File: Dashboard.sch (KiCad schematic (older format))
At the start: 24 parts, among them J24 ExtraGPIO_Conn, J25 UART_TP, J8 JTAG, SW10 RESET, U7 STM32F413RHTx, Y1 Crystal

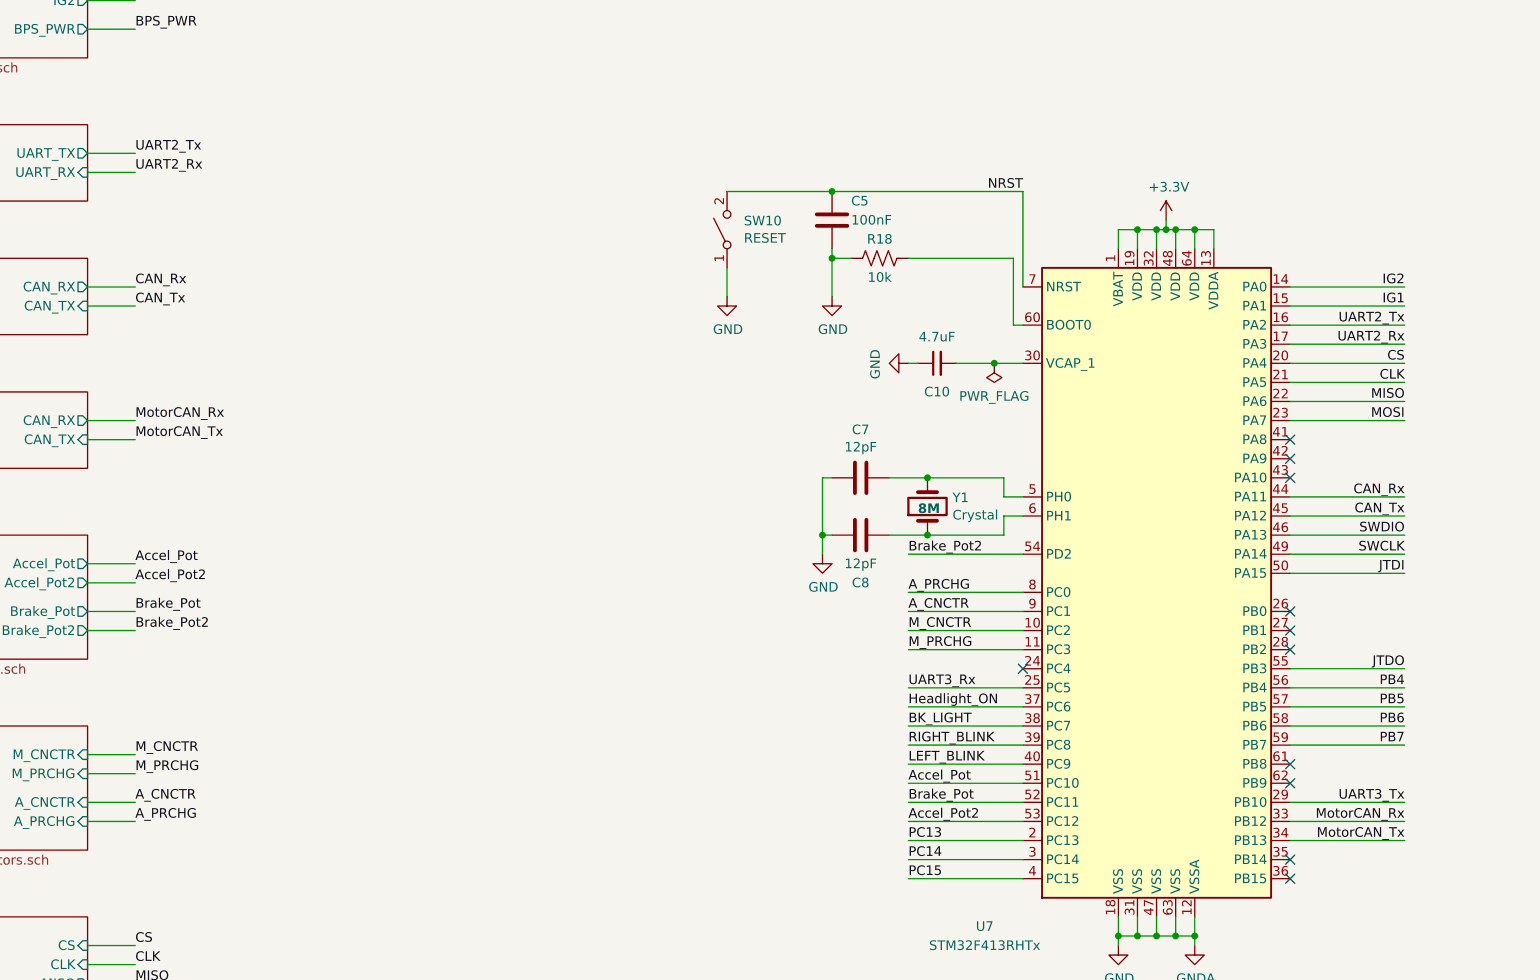
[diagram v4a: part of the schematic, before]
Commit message: USB Tx/Rx, Crystal Keepout, 12V Separation, Can2-Can3, Motor CAN bus labels, Power Input Protection Circuitry
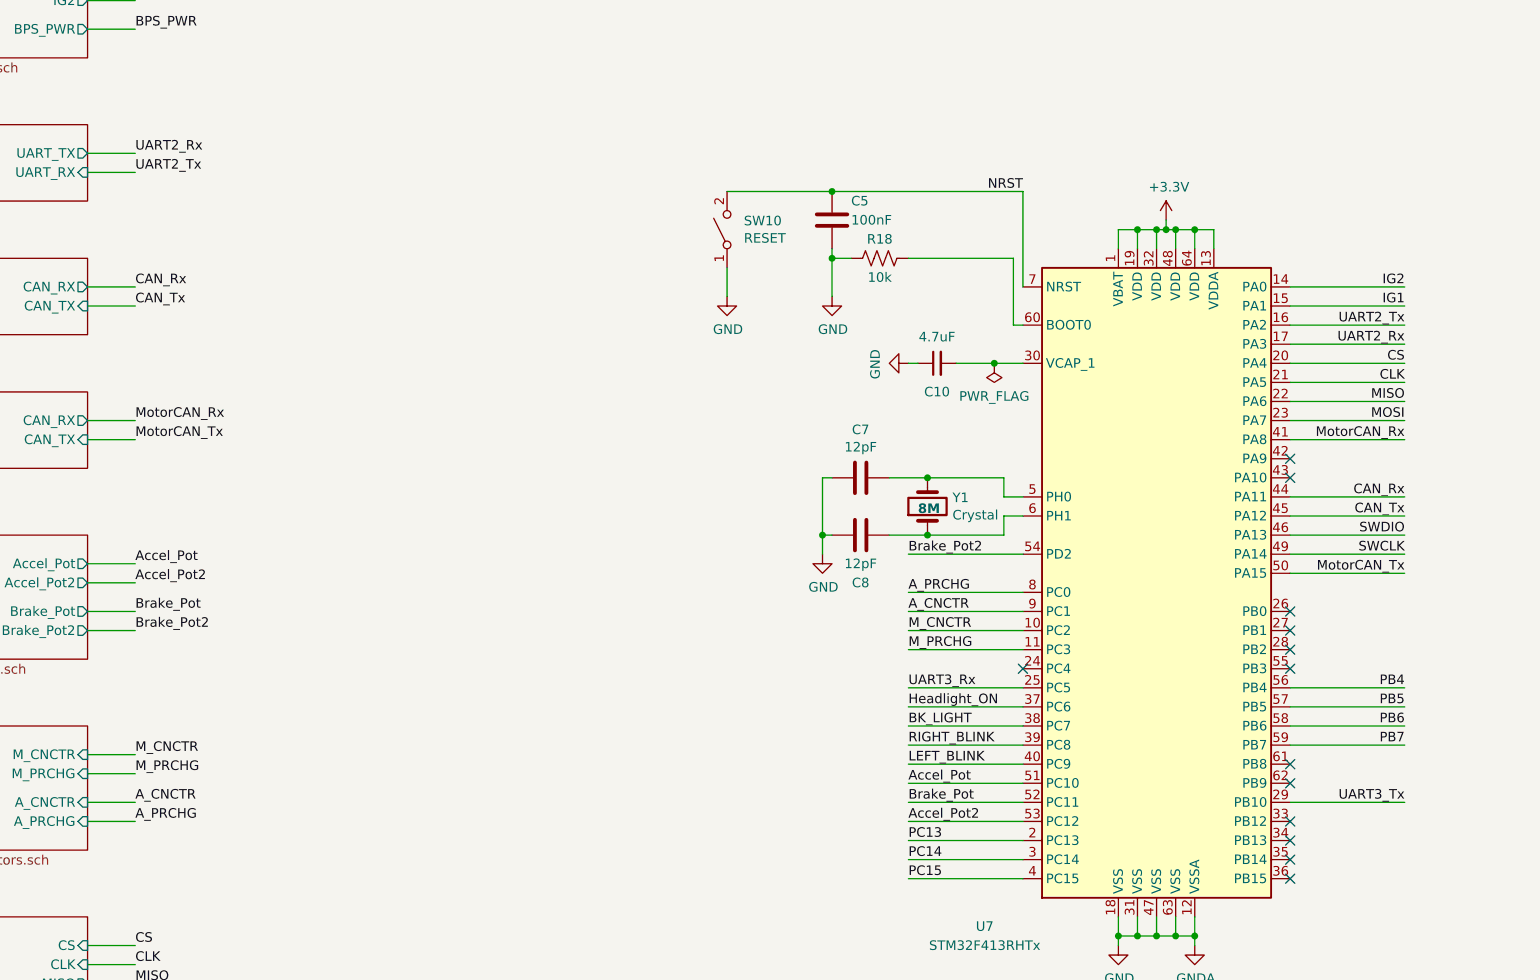
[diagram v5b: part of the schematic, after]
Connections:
- wire segments 169 -> 167
- no-connect marks 11 -> 13
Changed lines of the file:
@@
 Text Label 9600 6150 2    50   ~ 0
 SWCLK
-Text Label 9600 6250 2    50   ~ 0
-JTDI
-Text Label 9600 6750 2    50   ~ 0
-JTDO
 Wire Wire Line
 	9000 6150 9600 6150
@@
 	11900 4850 11900 5500
 Wire Wire Line
-	9000 6750 9600 6750
-Wire Wire Line
-	9000 6250 9600 6250
-Wire Wire Line
 	7000 6650 7600 6650
 Text Label 7000 6550 0    50   ~ 0
@@
 	8100 8150 8100 8200
 Connection ~ 8100 8150
-$Sheet
-S 1550 3900 1150 400
-U 5F7A9238
-F0 "USB" 50
-F1 "USB.sch" 50
-F2 "UART_RX" I R 2700 4150 50
-F3 "UART_TX" O R 2700 4050 50
-$EndSheet
 Wire Wire Line
 	7000 6850 7600 6850
-Text Label 2950 4050 0    50   ~ 0
+Text Label 2950 4150 0    50   ~ 0
 UART2_Tx
 Wire Wire Line
@@
 Wire Wire Line
 	2700 4150 2950 4150
-Text Label 2950 4150 0    50   ~ 0
+Text Label 2950 4050 0    50   ~ 0
 UART2_Rx
 Text Label 9600 5850 2    50   ~ 0
@@
 Text Label 2950 4850 0    50   ~ 0
 CAN_Tx
-Text Label 9600 7550 2    50   ~ 0
+Text Label 9600 5550 2    50   ~ 0
 MotorCAN_Rx
-Text Label 9600 7650 2    50   ~ 0
-MotorCAN_Tx
 Wire Wire Line
 	2700 5450 2950 5450
@@
 Wire Wire Line
 	11950 5300 11500 5300
-Wire Wire Line
-	9600 7550 9000 7550
-Wire Wire Line
-	9600 7650 9000 7650
 Wire Wire Line
 	7000 5150 7050 5150
@@
 NoConn ~ 9000 7850
 NoConn ~ 7600 6750
-NoConn ~ 9000 5550
 NoConn ~ 9000 5650
 NoConn ~ 9000 6450
-$Comp
-L MCU_ST_STM32F4:STM32F413RHTx U7
-U 1 1 5F09EDEE
-P 8300 6250
-F 0 "U7" H 7400 4400 50  0000 C CNN
-F 1 "STM32F413RHTx" H 7400 4300 50  0000 C CNN
-F 2 "Package_QFP:LQFP-64_10x10mm_P0.5mm" H 7700 4550 50  0001 R CNN
-F 3 "http://www.st.com/st-web-ui/static/active/en/resource/technical/document/datasheet/DM00282249.pdf" H 8300 6250 50  0001 C CNN
-	1    8300 6250
-	1    0    0    -1
-$EndComp
 Wire Wire Line
 	9600 5450 9000 5450
@@
 Wire Wire Line
 	2950 8600 2700 8600
+Text Label 9600 6250 2    50   ~ 0
+MotorCAN_Tx
+Wire Wire Line
+	9000 5550 9600 5550
+$Comp
+L MCU_ST_STM32F4:STM32F413RHTx U7
+U 1 1 5F09EDEE
+P 8300 6250
+F 0 "U7" H 7400 4400 50  0000 C CNN
+F 1 "STM32F413RHTx" H 7400 4300 50  0000 C CNN
+F 2 "Package_QFP:LQFP-64_10x10mm_P0.5mm" H 7700 4550 50  0001 R CNN
+F 3 "http://www.st.com/st-web-ui/static/active/en/resource/technical/document/datasheet/DM00282249.pdf" H 8300 6250 50  0001 C CNN
+	1    8300 6250
+	1    0    0    -1
+$EndComp
+NoConn ~ 9000 7550
+NoConn ~ 9000 7650
+NoConn ~ 9000 6750
+Wire Wire Line
+	9000 6250 9600 6250
+$Sheet
+S 1550 3900 1150 400
+U 5F7A9238
+F0 "USB" 50
+F1 "USB.sch" 50
+F2 "UART_RX" I R 2700 4150 50
+F3 "UART_TX" O R 2700 4050 50
+$EndSheet
 $EndSCHEMATC

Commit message: Connects pots to ADC pins and removes JTAG connections
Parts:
- J8: value JTAG -> SWD; footprint Connector_PinHeader_2.54mm:PinHeader_1x06_P2.54mm_Vertical -> Connector_PinHeader_2.54mm:PinHeader_1x04_P2.54mm_Vertical; symbol Connector_Generic:Conn_01x06 -> Connector_Generic:Conn_01x04
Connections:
- net labels removed: JTDI, JTDO
- wire segments 167 -> 165
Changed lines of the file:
@@
 Wire Wire Line
 	9000 6050 9600 6050
-$Comp
-L Connector_Generic:Conn_01x06 J8
-U 1 1 5F4102B2
-P 12150 5200
-F 0 "J8" H 12230 5192 50  0000 L CNN
-F 1 "JTAG" H 12230 5101 50  0000 L CNN
-F 2 "Connector_PinHeader_2.54mm:PinHeader_1x06_P2.54mm_Vertical" H 12150 5200 50  0001 C CNN
-F 3 "~" H 12150 5200 50  0001 C CNN
-	1    12150 5200
-	1    0    0    -1
-$EndComp
-Wire Wire Line
-	11950 5400 11500 5400
-Wire Wire Line
-	11500 5400 11500 5500
-Wire Wire Line
-	11950 5500 11900 5500
+Wire Wire Line
+	11950 5550 11550 5550
+Wire Wire Line
+	11550 5550 11550 5650
 $Comp
 L power:GND #PWR057
 U 1 1 5F4102BB
-P 11500 5500
-F 0 "#PWR057" H 11500 5250 50  0001 C CNN
-F 1 "GND" H 11505 5327 50  0000 C CNN
-F 2 "" H 11500 5500 50  0001 C CNN
-F 3 "" H 11500 5500 50  0001 C CNN
-	1    11500 5500
-	1    0    0    -1
-$EndComp
-$Comp
-L power:+3.3V #PWR058
-U 1 1 5F4102C1
-P 11900 4850
-F 0 "#PWR058" H 11900 4700 50  0001 C CNN
-F 1 "+3.3V" H 11915 5023 50  0000 C CNN
-F 2 "" H 11900 4850 50  0001 C CNN
-F 3 "" H 11900 4850 50  0001 C CNN
-	1    11900 4850
-	1    0    0    -1
-$EndComp
-Wire Wire Line
-	11900 4850 11900 5500
-Wire Wire Line
-	7000 6650 7600 6650
-Text Label 7000 6550 0    50   ~ 0
+P 11550 5650
+F 0 "#PWR057" H 11550 5400 50  0001 C CNN
+F 1 "GND" H 11555 5477 50  0000 C CNN
+F 2 "" H 11550 5650 50  0001 C CNN
+F 3 "" H 11550 5650 50  0001 C CNN
+	1    11550 5650
+	1    0    0    -1
+$EndComp
+Wire Wire Line
+	7000 6150 7600 6150
+Text Label 7000 7550 0    50   ~ 0
 M_CNCTR
-Text Label 7000 7350 0    50   ~ 0
+Text Label 7000 6350 0    50   ~ 0
 Accel_Pot
 Wire Wire Line
@@
 Text Label 7000 7050 0    50   ~ 0
 BK_LIGHT
-Text Label 7000 7450 0    50   ~ 0
+Text Label 7000 6450 0    50   ~ 0
 Brake_Pot
 Text Label 7000 6950 0    50   ~ 0
@@
 	9750 2900 9750 2800
 Connection ~ 9150 2900
-Text Label 7000 7550 0    50   ~ 0
+Text Label 7000 6550 0    50   ~ 0
 Accel_Pot2
-Text Label 7000 6150 0    50   ~ 0
+Text Label 7000 6650 0    50   ~ 0
 Brake_Pot2
 Wire Wire Line
-	7000 6150 7600 6150
-Wire Wire Line
-	7000 7550 7600 7550
-Wire Wire Line
-	7000 7350 7600 7350
-Wire Wire Line
-	7000 7450 7600 7450
+	7000 6650 7600 6650
+Wire Wire Line
+	7000 6550 7600 6550
+Wire Wire Line
+	7000 6350 7600 6350
+Wire Wire Line
+	7000 6450 7600 6450
 Text Label 7000 7250 0    50   ~ 0
 LEFT_BLINK
@@
 Wire Wire Line
 	9600 5050 9000 5050
-Text Label 11500 5000 0    50   ~ 0
+Text Label 11550 5450 0    50   ~ 0
 SWDIO
-Text Label 11500 5300 0    50   ~ 0
+Text Label 11550 5350 0    50   ~ 0
 SWCLK
-Text Label 11500 5100 0    50   ~ 0
-JTDI
-Text Label 11500 5200 0    50   ~ 0
-JTDO
-Wire Wire Line
-	11950 5000 11500 5000
-Wire Wire Line
-	11950 5100 11500 5100
-Wire Wire Line
-	11950 5200 11500 5200
-Wire Wire Line
-	11950 5300 11500 5300
+Wire Wire Line
+	11950 5450 11550 5450
+Wire Wire Line
+	11950 5350 11550 5350
 Wire Wire Line
 	7000 5150 7050 5150
@@
 	2700 7200 2950 7200
 Wire Wire Line
-	7600 6550 7000 6550
-Text Label 7000 6650 0    50   ~ 0
+	7600 7550 7000 7550
+Text Label 7000 6150 0    50   ~ 0
 M_PRCHG
 Wire Wire Line
-	7000 6450 7600 6450
-Text Label 7000 6450 0    50   ~ 0
+	7000 7450 7600 7450
+Text Label 7000 7450 0    50   ~ 0
 A_CNCTR
 Wire Wire Line
-	7600 6350 7000 6350
-Text Label 7000 6350 0    50   ~ 0
+	7600 7350 7000 7350
+Text Label 7000 7350 0    50   ~ 0
 A_PRCHG
 Text Label 9600 7150 2    50   ~ 0
@@
 F3 "UART_TX" O R 2700 4050 50
 $EndSheet
+$Comp
+L power:+3.3V #PWR058
+U 1 1 5F4102C1
+P 11550 5150
+F 0 "#PWR058" H 11550 5000 50  0001 C CNN
+F 1 "+3.3V" H 11565 5323 50  0000 C CNN
+F 2 "" H 11550 5150 50  0001 C CNN
+F 3 "" H 11550 5150 50  0001 C CNN
+	1    11550 5150
+	1    0    0    -1
+$EndComp
+$Comp
+L Connector_Generic:Conn_01x04 J8
+U 1 1 5F4102B2
+P 12150 5350
+F 0 "J8" H 12230 5342 50  0000 L CNN
+F 1 "SWD" H 12230 5251 50  0000 L CNN
+F 2 "Connector_PinHeader_2.54mm:PinHeader_1x04_P2.54mm_Vertical" H 12150 5350 50  0001 C CNN
+F 3 "~" H 12150 5350 50  0001 C CNN
+	1    12150 5350
+	1    0    0    -1
+$EndComp
+Wire Wire Line
+	11950 5250 11550 5250
+Wire Wire Line
+	11550 5250 11550 5150
 $EndSCHEMATC

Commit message: removes the isp
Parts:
- LOGO1, LOGO2: symbol utsvt-misc:Logo_Placeholder -> Dashboard-rescue:Logo_Placeholder-utsvt-misc
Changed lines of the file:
@@
 	11950 6950 11500 6950
 $Comp
-L utsvt-misc:Logo_Placeholder LOGO2
+L Dashboard-rescue:Logo_Placeholder-utsvt-misc LOGO2
 U 1 1 5F7C8578
 P 12000 9500
@@
 $EndComp
 $Comp
-L utsvt-misc:Logo_Placeholder LOGO1
+L Dashboard-rescue:Logo_Placeholder-utsvt-misc LOGO1
 U 1 1 5F7C966B
 P 12000 9200

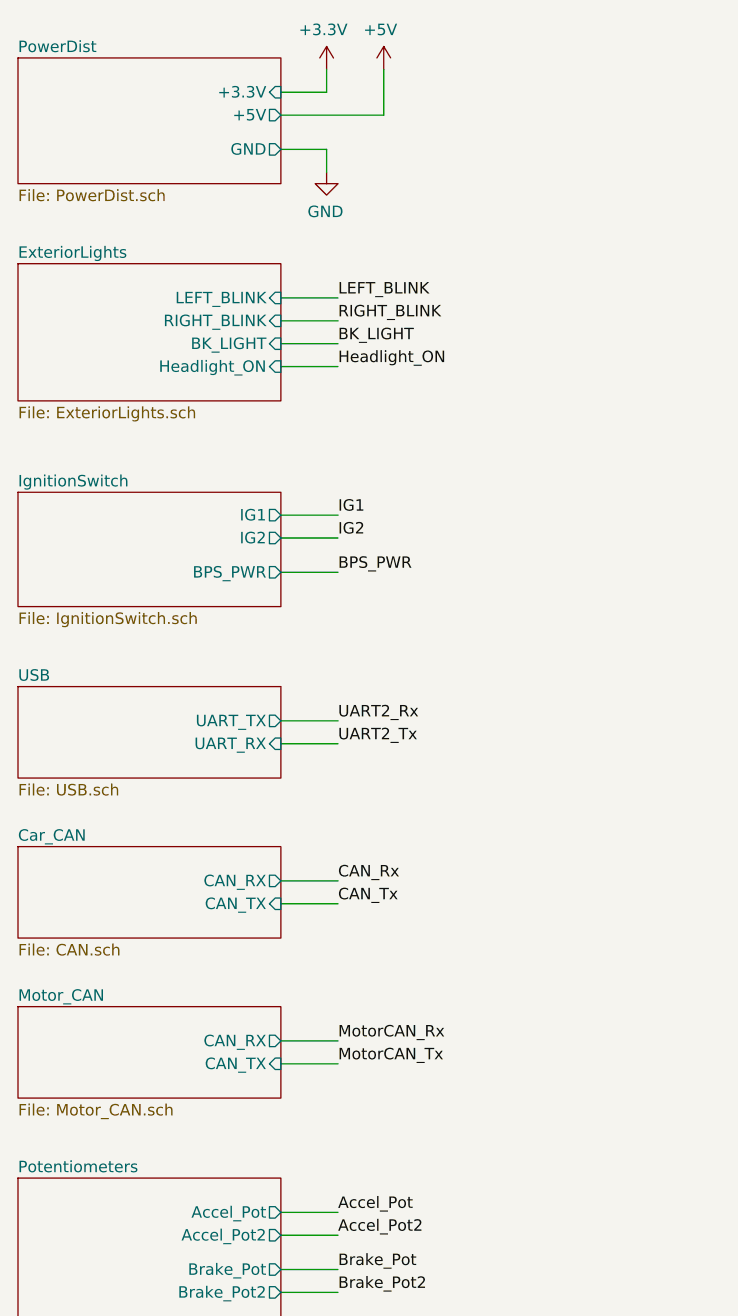
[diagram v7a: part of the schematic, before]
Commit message: Changes the layout of the board, adds resistors for ignition switch, and gives motar can isolated +12v, still need to change resistor value for the isolated +12v(didnt remember how to find the value)
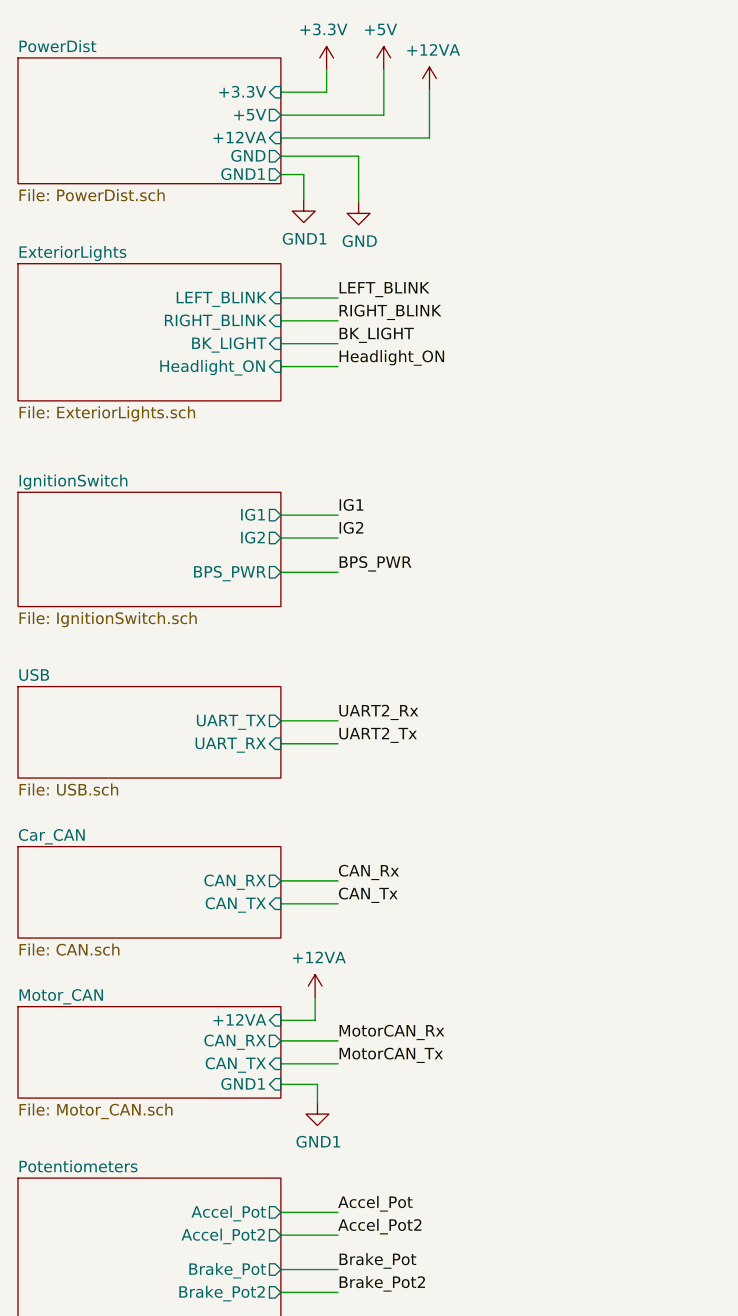
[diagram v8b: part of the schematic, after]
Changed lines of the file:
@@
 F0 "PowerDist" 50
 F1 "PowerDist.sch" 50
-F2 "GND" O R 2700 1550 50
+F2 "GND" O R 2700 1580 50
 F3 "+5V" O R 2700 1400 50
 F4 "+3.3V" I R 2700 1300 50
+F5 "+12VA" I R 2700 1500 50
+F6 "GND1" O R 2700 1660 50
 $EndSheet
 $Comp
@@
 	-1   0    0    -1
 $EndComp
-$Comp
-L power:GND #PWR073
-U 1 1 5F2551FE
-P 2900 1650
-F 0 "#PWR073" H 2900 1400 50  0001 C CNN
-F 1 "GND" H 2905 1477 50  0000 C CNN
-F 2 "" H 2900 1650 50  0001 C CNN
-F 3 "" H 2900 1650 50  0001 C CNN
-	1    2900 1650
-	-1   0    0    -1
-$EndComp
 Wire Wire Line
 	2700 1400 3150 1400
@@
 Wire Wire Line
 	2900 1300 2900 1200
-Wire Wire Line
-	2700 1550 2900 1550
-Wire Wire Line
-	2900 1550 2900 1650
 $Comp
 L power:+3.3V #PWR051
@@
 	-1   0    0    -1
 $EndComp
-$Sheet
-S 1550 5300 1150 400
-U 5F6018FB
-F0 "Motor_CAN" 50
-F1 "Motor_CAN.sch" 50
-F2 "CAN_TX" I R 2700 5550 50
-F3 "CAN_RX" O R 2700 5450 50
-$EndSheet
 Wire Wire Line
 	7600 7250 7000 7250
@@
 Wire Wire Line
 	11550 5250 11550 5150
+Wire Wire Line
+	2700 1500 3350 1500
+Wire Wire Line
+	3350 1290 3350 1500
+$Sheet
+S 1550 5300 1150 400
+U 5F6018FB
+F0 "Motor_CAN" 50
+F1 "Motor_CAN.sch" 50
+F2 "CAN_TX" I R 2700 5550 50
+F3 "CAN_RX" O R 2700 5450 50
+F4 "+12VA" I R 2700 5360 50
+F5 "GND1" I R 2700 5640 50
+$EndSheet
+Wire Wire Line
+	2700 5360 2850 5360
+Wire Wire Line
+	2850 5360 2850 5260
+Wire Wire Line
+	2700 5640 2860 5640
+Wire Wire Line
+	2860 5640 2860 5720
+Wire Wire Line
+	2700 1660 2800 1660
+Wire Wire Line
+	2800 1660 2800 1770
+$Comp
+L power:GND #PWR014
+U 1 1 619AD7C1
+P 3040 1780
+F 0 "#PWR014" H 3040 1530 50  0001 C CNN
+F 1 "GND" H 3045 1607 50  0000 C CNN
+F 2 "" H 3040 1780 50  0001 C CNN
+F 3 "" H 3040 1780 50  0001 C CNN
+	1    3040 1780
+	1    0    0    -1
+$EndComp
+Wire Wire Line
+	3040 1780 3040 1580
+Wire Wire Line
+	2700 1580 3040 1580
+$Comp
+L power:+12VA #PWR04
+U 1 1 619BA3E5
+P 2850 5260
+F 0 "#PWR04" H 2850 5110 50  0001 C CNN
+F 1 "+12VA" H 2865 5433 50  0000 C CNN
+F 2 "" H 2850 5260 50  0001 C CNN
+F 3 "" H 2850 5260 50  0001 C CNN
+	1    2850 5260
+	1    0    0    -1
+$EndComp
+$Comp
+L power:GND1 #PWR07
+U 1 1 619CCBE3
+P 2860 5720
+F 0 "#PWR07" H 2860 5470 50  0001 C CNN
+F 1 "GND1" H 2865 5547 50  0000 C CNN
+F 2 "" H 2860 5720 50  0001 C CNN
+F 3 "" H 2860 5720 50  0001 C CNN
+	1    2860 5720
+	1    0    0    -1
+$EndComp
+$Comp
+L power:GND1 #PWR03
+U 1 1 619CE2A5
+P 2800 1770
+F 0 "#PWR03" H 2800 1520 50  0001 C CNN
+F 1 "GND1" H 2805 1597 50  0000 C CNN
+F 2 "" H 2800 1770 50  0001 C CNN
+F 3 "" H 2800 1770 50  0001 C CNN
+	1    2800 1770
+	1    0    0    -1
+$EndComp
+$Comp
+L power:+12VA #PWR?
+U 1 1 61936106
+P 3350 1290
+F 0 "#PWR?" H 3350 1140 50  0001 C CNN
+F 1 "+12VA" H 3365 1463 50  0000 C CNN
+F 2 "" H 3350 1290 50  0001 C CNN
+F 3 "" H 3350 1290 50  0001 C CNN
+	1    3350 1290
+	1    0    0    -1
+$EndComp
 $EndSCHEMATC
